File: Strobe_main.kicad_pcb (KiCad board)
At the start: 4 copper layers, 100 x 100 mm, 172 parts, among them J1001 Header, J302 T44007, J303 T44007, J304 10146581-060_M, J305 T44007, J306 T44007, J501 HX JN1.27-2x5P ZZ H4.9, J701 ZHOURI DC3, J801 Molex 430452427, J901 Header, Q301 MPF3N150, Q302 IXYH55N120, Q303 IXYH55N120, Q304 IXYH55N120, Q305 IXYH55N120, U100 LM217MDT, U101 AMS1117-3.3, U102 AMS1117-3.3, U301 IRS2184, U401 TSV912IDT, U501 STM32G431K8Tx, U601 ISO1541, U602 ISO6741, Y501 20 MHz

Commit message: Sch update complete, ERC OK
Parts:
- removed J801: Molex 430452427, Connector_Molex:Molex_Micro-Fit_3.0_43045-2412_2x12_P3.00mm_Vertical
- removed Mod100: WB0524S-1W, Personal:WB___S-1W
- removed Mod101: WB0505S-1W, Personal:WB___S-1W
- added J800: Molex 430451227, Connector_Molex:Molex_Micro-Fit_3.0_43045-1212_2x06_P3.00mm_Vertical, F.Cu at (273.2, 46.1)
- added PS100: B0505S-2W, Personal:DCDC_converter_THT_BxxxxS-2W, F.Cu at (289.2, 115.4)
- added PS101: B0524S-2W, Personal:DCDC_converter_THT_BxxxxS-2W, F.Cu at (289.2, 124.5)
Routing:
- net unconnected-(J801-Pin_5-Pad5): track 36.2 -> 0.00 mm
- net /Block Diagram/Vbus_ctrl: track 109.5 -> 76.6 mm

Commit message: Placement started
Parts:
- C102, C103, C104, C105, C303, C304, C307, C309, C401, C402, C501, C502, C503, C504, C505, C506, C603, C604, D302, D303, D304, D310, D401, D402, D403, R101, R303, R304, R306, R309, R311, R312, R313, R314, R315, R316, R317, R323, R328, R329, R332, R336, R337, R401, R402, R501, R502, R507, R609, R610, R611, R612, R613, R614, R615, R616, R617, R618, R619, R701, R702, TP301, TP302, TP303, TP304, TP309, TP310, TP311, TP312, TP313, TP501, TP502, TP503, TP504, TP505, TP506, TP507, TP508, TP509, TP510, TP511, TP512, TP514, TP515, TP516, TP517, U401, U501, U602, Y501: moved to F.Cu
- moved C100 194.4 mm to (164.2, 199.4)
- moved R316 190.5 mm to (391.6, 99.7), turned to 0 degrees
- moved C106 189.4 mm to (168.5, 199.4)
- moved C107 189.4 mm to (168.5, 201.9)
- moved R100 189.4 mm to (168.5, 206.9)
- moved R313 189.4 mm to (391.6, 92.2), turned to 0 degrees
- moved TP304 189.0 mm to (392.8, 84.9)
- moved R317 188.8 mm to (391.6, 102.2), turned to 0 degrees
- moved U101 188.2 mm to (176.3, 214.0)
- moved C304 186.1 mm to (387.2, 97.2), turned to 0 degrees
- moved R311 175.3 mm to (382.6, 86.3)
- moved R309 172.4 mm to (382.6, 79.7)
- moved U100 169.5 mm to (177.6, 202.3)
- moved R310 168.3 mm to (321.8, 82.0), turned to 0 degrees
- moved R312 167.9 mm to (333.6, 88.4), turned to 0 degrees
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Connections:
- J800 pad 2: /Block Diagram/MCU/SUP_TX -> /Block Diagram/SH0
- J800 pad 3: /Block Diagram/SH0 -> unconnected-(J800-Pin_3-Pad3)
- J800 pad 8: /Block Diagram/SH5 -> unconnected-(J800-Pin_8-Pad8)
- J800 pad 9: Earth -> unconnected-(J800-Pin_9-Pad9)
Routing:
- net /Block Diagram/SH3: track 337.0 -> 0.00 mm, vias 14 -> 0
- net /Block Diagram/SH0: track 213.5 -> 0.00 mm, vias 77 -> 0
- net /Block Diagram/Lamp driver/DRV_OUT: track 121.8 -> 0.00 mm, vias 2 -> 0
- net /Block Diagram/S1k: track 103.8 -> 0.53 mm
- net /Block Diagram/SL3: track 90.2 -> 0.00 mm, vias 1 -> 0
- net /Block Diagram/SH20: track 88.7 -> 0.00 mm, vias 1 -> 0
- net (no net): track 80.1 -> 0.00 mm, vias 2 -> 0
- net /Block Diagram/MCU/HV_SWDIO: track 79.7 -> 0.00 mm
- net /Block Diagram/Vbus_ctrl: track 76.6 -> 0.00 mm, vias 1 -> 0
- net /Block Diagram/MCU/HV_EXT_EN: track 72.4 -> 0.00 mm, vias 2 -> 0
- net /Block Diagram/MCU/HV_NRST: track 70.4 -> 0.00 mm, vias 2 -> 0
- net /Block Diagram/MCU/HV_SWDCLK: track 67.3 -> 0.00 mm
- net /Block Diagram/MCU/HV_RX: track 64.5 -> 0.00 mm, vias 2 -> 0
- net /Block Diagram/MCU/HV_TX: track 62.1 -> 0.00 mm
- net /Block Diagram/SH5: track 60.4 -> 0.00 mm, vias 2 -> 0
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- removed copper zone on In1.Cu, net /Block Diagram/GND
- removed copper zone on In2.Cu, net /Block Diagram/GND
- removed copper zone on B.Cu, net /Block Diagram/Lamp driver/LMP
- removed copper zone on F.Cu, net /Block Diagram/Lamp driver/LMP
- removed copper zone on In1.Cu, net /Block Diagram/Lamp driver/LMP
- removed copper zone on In2.Cu, net /Block Diagram/Lamp driver/LMP
- removed copper zone on B.Cu, net /Block Diagram/Lamp driver/Mon_IL
- removed copper zone on In1.Cu, net /Block Diagram/Lamp driver/Mon_IL
- removed copper zone on In2.Cu, net /Block Diagram/Lamp driver/Mon_IL
- removed copper zone on F.Cu, net /Block Diagram/Lamp driver/TP_PRI
- removed copper zone on B.Cu, net /Block Diagram/S1k
- removed copper zone on F.Cu, net /Block Diagram/S1k
- removed copper zone on In1.Cu, net /Block Diagram/S1k
- removed copper zone on In2.Cu, net /Block Diagram/S1k
- removed copper zone on B.Cu, net /Block Diagram/SH0
- removed copper zone on In1.Cu, net /Block Diagram/SH0
- removed copper zone on In2.Cu, net /Block Diagram/SH0
- removed copper zone on B.Cu, net /Block Diagram/SH3
- removed copper zone on F.Cu, net /Block Diagram/SH3
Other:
- outline, holes or cut-outs redrawn

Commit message: Placement 50%
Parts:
- removed J501: HX JN1.27-2x5P ZZ H4.9, Personal:HX JN1.27-2x5P ZZ H4.9
- removed R302, R304: NF, Resistor_SMD:R_1206_3216Metric_Pad1.30x1.75mm_HandSolder
- removed R315, R317: NF, Resistor_SMD:R_0603_1608Metric_Pad0.98x0.95mm_HandSolder
- removed TP301: TestPoint, TestPoint:TestPoint_THTPad_D1.0mm_Drill0.5mm
- C100, C101, C102, C103, C104, C105, C106, C107, C108, C307, C309, C310, C601, C602, D303, D304, D305, D309, D310, R100, R101, R319, R332, R336, R601, R602, R603, R604, R605, R606, R607, R608, R701, R702, TP309, U100, U101, U102, U601: moved to B.Cu
- moved TP304 222.8 mm to (172.2, 116.5), turned to -90 degrees
- moved R316 219.5 mm to (172.5, 112.5)
- moved R313 215.8 mm to (176.5, 109.5)
- moved C304 211.0 mm to (176.5, 107.5), turned to 180 degrees
- moved R309 208.8 mm to (177.5, 118.5), turned to -90 degrees
- moved R311 206.9 mm to (177.5, 113.5), turned to -90 degrees
- moved R306 203.9 mm to (174.5, 122.5), turned to -90 degrees
- moved R303 203.0 mm to (177.5, 125.5), turned to -90 degrees
- moved R401 183.1 mm to (133.5, 124.2), turned to 90 degrees
- moved C402 180.8 mm to (137.5, 124.2), turned to -90 degrees
- moved U401 180.3 mm to (138.5, 114.1), turned to 90 degrees
- moved R402 180.2 mm to (135.5, 124.2), turned to 90 degrees
- moved C401 179.0 mm to (134.5, 112.1), turned to -90 degrees
- moved D401 178.5 mm to (140.5, 124.1), turned to 90 degrees
- moved TP303 174.4 mm to (162.7, 128.6), turned to -90 degrees
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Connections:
- D304 pad 1: /Block Diagram/Lamp driver/TP_PRI -> Net-(D304-K)
- D304 pad 2: Net-(D304-A) -> /Block Diagram/Lamp driver/TP_COM
- R332 pad 1: /Block Diagram/Lamp driver/TP_COM -> Net-(D304-K)
- R332 pad 2: Net-(D304-A) -> /Block Diagram/Lamp driver/TP_PRI
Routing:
- net /Block Diagram/S1k: track 0.53 -> 148.1 mm
- net /Block Diagram/Lamp driver/DRV_OUT: track 0.00 -> 107.5 mm, vias 0 -> 1
- net /Block Diagram/Lamp driver/LMP: track 0.00 -> 83.9 mm
- net /Block Diagram/Lamp driver/TP_PRI: track 0.00 -> 72.2 mm
- net /Block Diagram/SH20: track 0.00 -> 62.8 mm, vias 0 -> 1
- net /Block Diagram/SH0: track 0.00 -> 56.5 mm, vias 0 -> 13
- net /Block Diagram/SL3: track 0.00 -> 37.4 mm, vias 0 -> 3
- net /Block Diagram/SH3: track 0.00 -> 35.1 mm
- net /Block Diagram/Lamp driver/TP_COM: track 0.00 -> 24.2 mm
- net /Block Diagram/Optical isolation/LV_SWDCLK: track 0.00 -> 20.8 mm
- net /Block Diagram/GND: track 0.00 -> 19.6 mm, vias 0 -> 8
- net Net-(J701-Pin_2): track 0.00 -> 18.9 mm
- net /Block Diagram/Lamp driver/TP_REF: track 0.00 -> 17.6 mm
- net /Block Diagram/Optical isolation/LV_SWDIO: track 0.00 -> 17.5 mm
- net /Block Diagram/Lamp driver/G_TP_DRV: track 0.00 -> 15.7 mm
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- added copper zone on In1.Cu, net /Block Diagram/GND
- added copper zone on F.Cu, net /Block Diagram/Lamp driver/LMP
- added copper zone on In1.Cu, net /Block Diagram/Lamp driver/LMP
- added copper zone on B.Cu, net /Block Diagram/Lamp driver/Mon_IL
- added copper zone on In2.Cu, net /Block Diagram/Lamp driver/Mon_IL
- added copper zone on B.Cu, net /Block Diagram/SH0
- added copper zone on In1.Cu, net /Block Diagram/SH0
- added copper zone on In2.Cu, net /Block Diagram/SL3

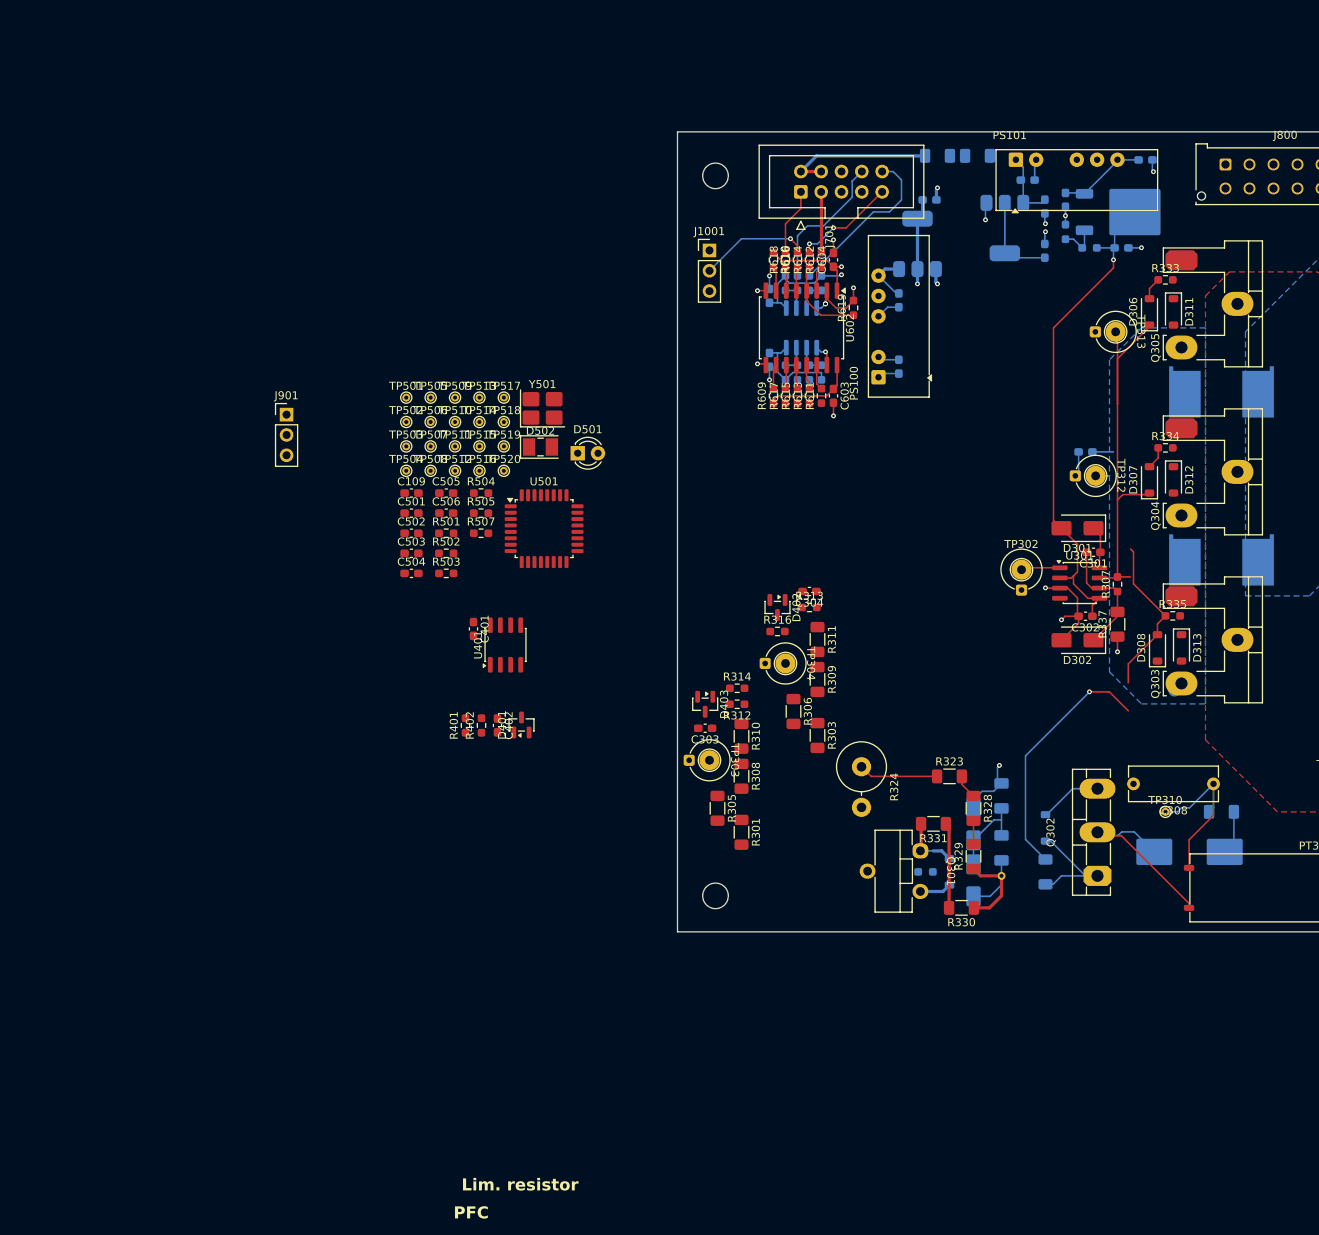
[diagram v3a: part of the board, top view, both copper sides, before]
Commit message: Updated pulse transofrmer circuit
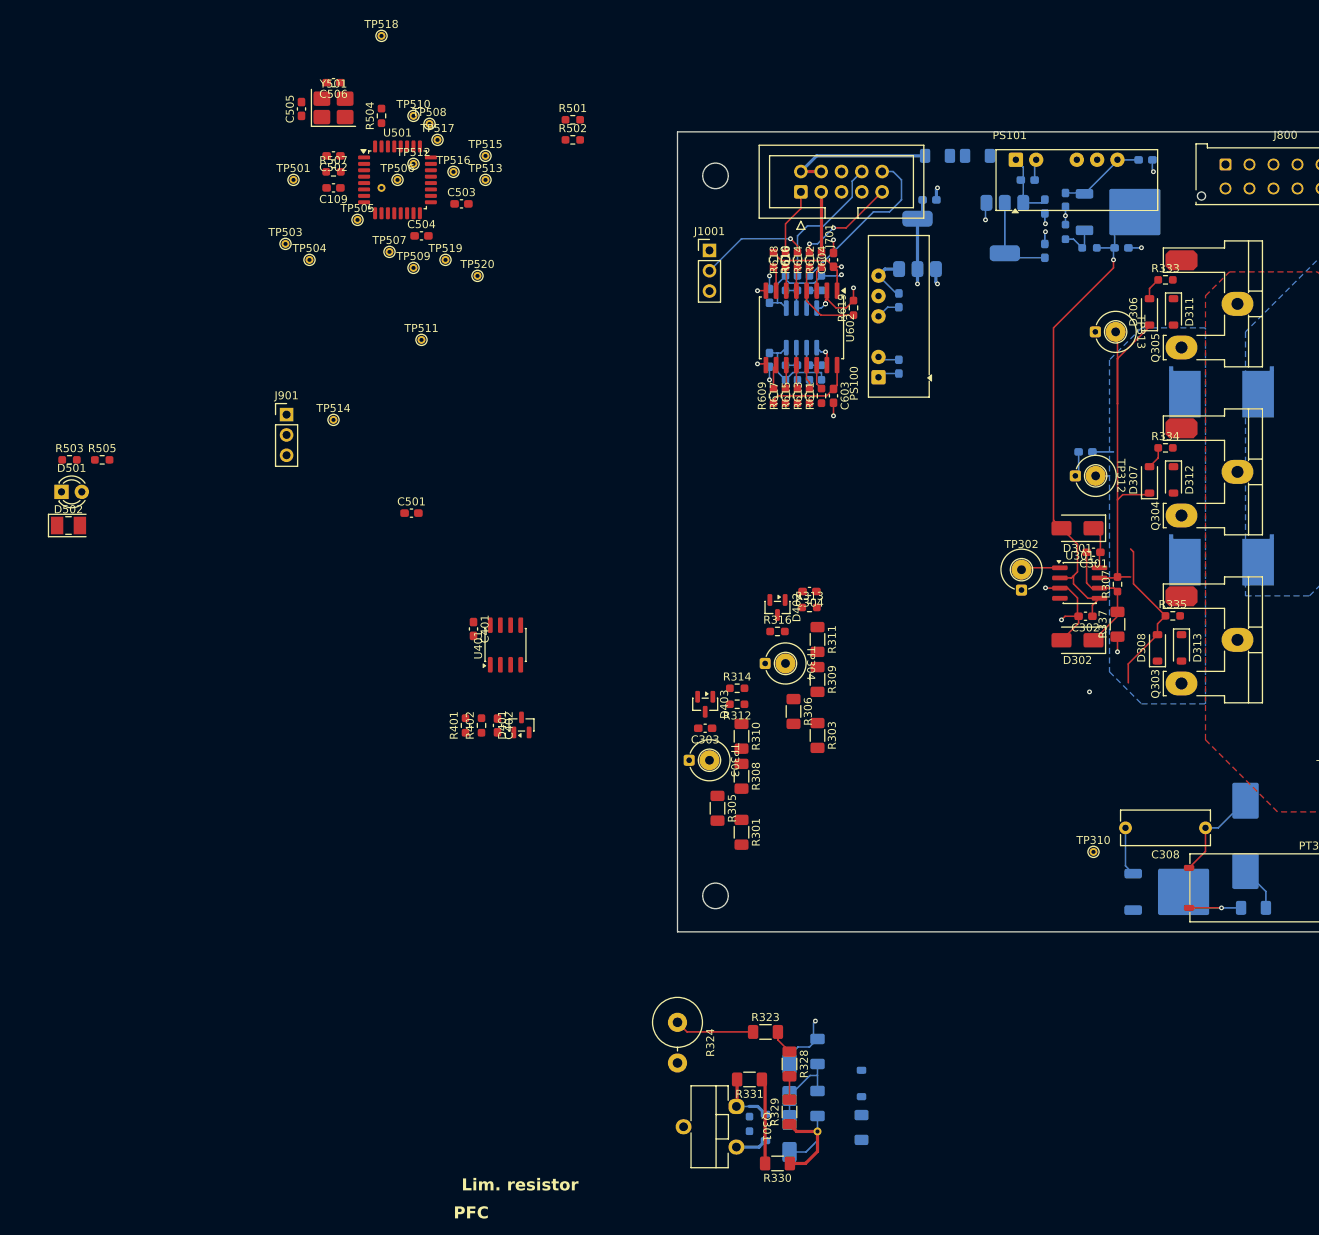
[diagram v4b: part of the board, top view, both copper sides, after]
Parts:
- removed Q302: IXYH55N120, Personal:TO-247_small_p1
- added Q100: MDT7N65, Package_TO_SOT_SMD:TO-252-2, B.Cu at (222.0, 145.0)
- TP502: moved to B.Cu
- moved D501 64.7 mm to (83.0, 95.0)
- moved D502 59.8 mm to (83.9, 99.2)
- moved C506 55.6 mm to (117.0, 43.9), turned to 180 degrees
- moved R502 54.0 mm to (146.9, 51.0)
- moved R501 54.0 mm to (146.9, 48.5)
- moved C505 51.3 mm to (113.0, 47.1), turned to 90 degrees
- moved TP518 50.6 mm to (123.0, 38.0)
- moved R503 49.2 mm to (84.0, 91.0)
- moved R507 48.8 mm to (117.0, 55.0)
- moved R504 48.8 mm to (123.0, 48.0), turned to 90 degrees
- moved C502 48.2 mm to (117.0, 53.0), turned to 180 degrees
- moved R505 47.8 mm to (88.1, 91.0)
- moved U501 47.3 mm to (125.0, 56.0)
- moved Y501 45.8 mm to (117.0, 47.0)
- moved C503 44.1 mm to (133.0, 59.0)
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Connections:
- D304 pad 1: Net-(D304-K) -> /Block Diagram/Lamp driver/TP_PRI
- D304 pad 2: /Block Diagram/Lamp driver/TP_COM -> /Block Diagram/Lamp driver/TP_INT
- R332 pad 1: Net-(D304-K) -> /Block Diagram/Lamp driver/TP_COM
- R332 pad 2: /Block Diagram/Lamp driver/TP_PRI -> /Block Diagram/Lamp driver/TP_INT
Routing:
- net /Block Diagram/Lamp driver/DRV_OUT: track 107.5 -> 76.3 mm
- net /Block Diagram/Lamp driver/TP_PRI: track 72.2 -> 41.2 mm
- net /Block Diagram/Lamp driver/G_TP_DRV: track 15.7 -> 0.00 mm
- net /Block Diagram/Lamp driver/TP_COM: track 24.2 -> 12.1 mm, vias 0 -> 1
- net /Block Diagram/Lamp driver/LMP: track 83.9 -> 73.2 mm
- net /Block Diagram/Lamp driver/TP_INT: track 0.00 -> 5.66 mm
- net Net-(D304-K): track 5.48 -> 0.00 mm
- net /Block Diagram/SH0: track 56.5 -> 53.6 mm
- net /Block Diagram/Lamp driver/Mon_IL: track 7.53 -> 6.27 mm
